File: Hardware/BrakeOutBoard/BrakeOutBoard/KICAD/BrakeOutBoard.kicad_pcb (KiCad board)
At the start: 2 copper layers, 63 x 83 mm, 56 parts, among them J1 To USB converter, J10 WhiperWater, J11 BrakePads, J12 BrakeFluid, J13 Door_R, J14 OilPresure, J15 Door_S, J16 TFT_CS, J17 TFT_DC, J18 TFT_GND, J19 TFT_SLK, J2 K15, J20 Conn_01x19_Socket, J21 TFT_MOSI, J22 TFT_RST, J24 Reset, J25 Can_H, J26 Memory, J27 Can_L, J28 Trunk, J29 Mode, J3 K30, J4 TFT_5V, J5 Conn_01x19_Socket, J6 K31, J7 Coolant, J8 oilSensor, J9 MotorCap, Q1 MMDT3904, Q2 LBSS84LT1G, U1 LTV-847, U101 SN65HVD230DR, U2 LTV-847, U3 LVT 817, U4 LTV-847

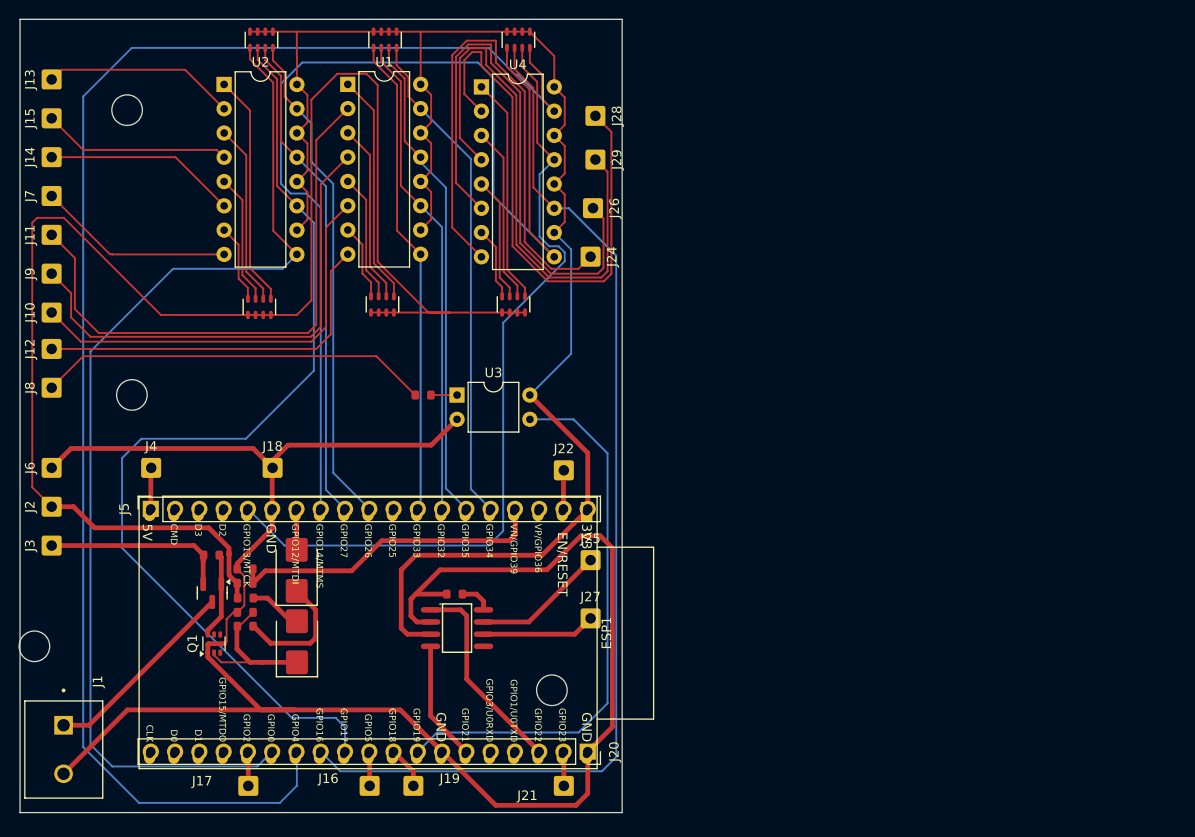
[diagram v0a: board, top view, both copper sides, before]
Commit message: Add files via upload
Forgot to include connector for Oil Level LED
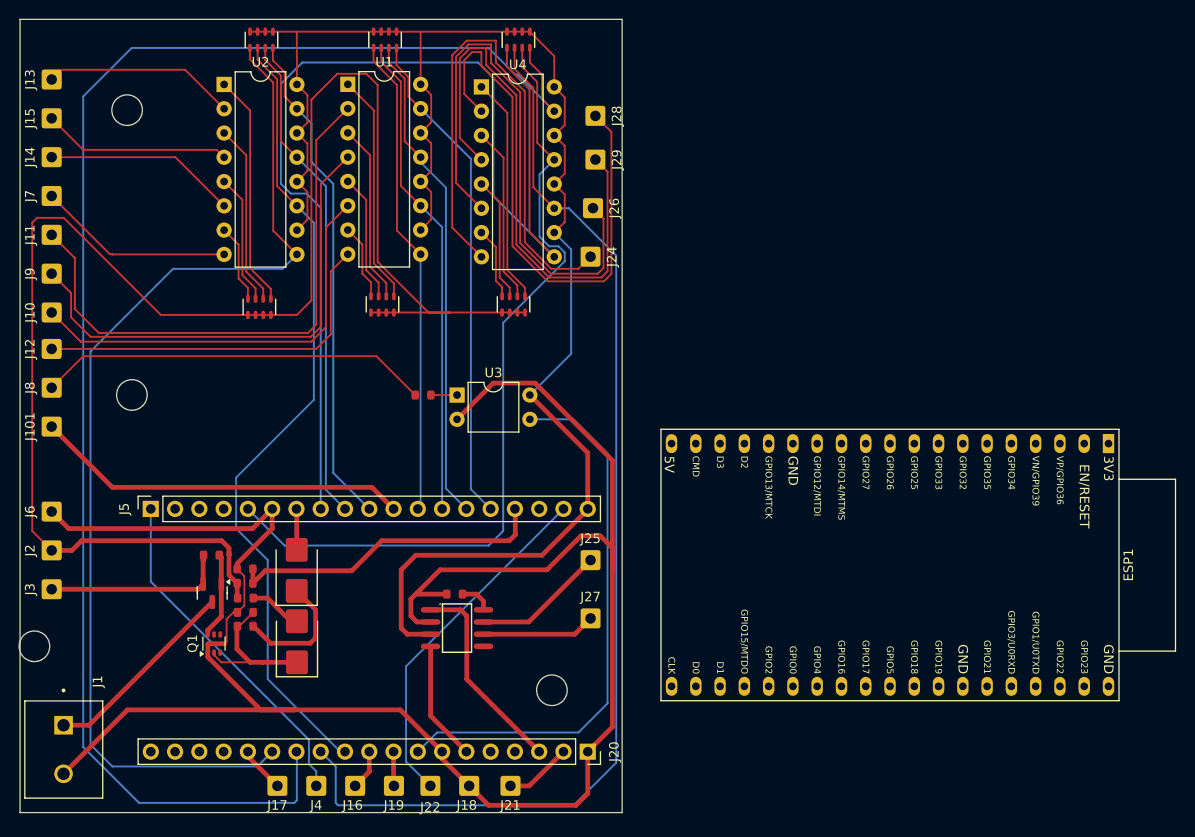
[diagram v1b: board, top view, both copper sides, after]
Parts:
- added J101: O_Lev_LED, Connector_Wire:SolderWire-0.5sqmm_1x01_D0.9mm_OD2.1mm, F.Cu at (127.3, 115.2)
- moved ESP1 55.1 mm to (237.9, 117.0)
- moved J18 39.1 mm to (171.0, 152.8), turned to 180 degrees
- moved J4 37.5 mm to (155.0, 152.8)
- moved J22 35.9 mm to (166.9, 152.8), turned to 180 degrees
- moved J21 5.59 mm to (175.3, 152.8)
- moved J2 4.57 mm to (127.3, 128.2)
- moved J6 4.57 mm to (127.3, 124.1)
- moved J3 4.57 mm to (127.3, 132.2)
- moved J17 3.05 mm to (150.9, 152.8)
- moved J19 2.03 mm to (163.1, 152.8)
- moved J16 1.52 mm to (159.1, 152.8)
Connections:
- J5 pad 11: unconnected-(J5-Pin_11-Pad11) -> Net-(J101-Pin_1)
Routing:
- net Net-(J101-Pin_1): track 0.00 -> 39.3 mm
- net Net-(J22-Pin_1): track 4.00 -> 36.9 mm
- net Net-(J4-Pin_1): track 4.25 -> 36.2 mm
- net Pin 10 Green Connector (Oil Presure): track 103.1 -> 84.4 mm
- net GND: track 202.4 -> 210.0 mm
- net Pin 23 Green Connector (Memory switch): track 111.9 -> 117.4 mm
- net /K15: track 164.8 -> 168.4 mm
- net Net-(J20-Pin_2): track 3.54 -> 7.03 mm
- net Net-(J17-Pin_1): track 3.54 -> 4.86 mm
- net (Trunk): track 158.9 -> 159.8 mm
- net Net-(J19-Pin_1): track 4.44 -> 3.60 mm
- net Net-(J16-Pin_1): track 3.54 -> 4.20 mm
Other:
- board text removed: "Can Modul"
